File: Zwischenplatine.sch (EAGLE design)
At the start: 12 parts

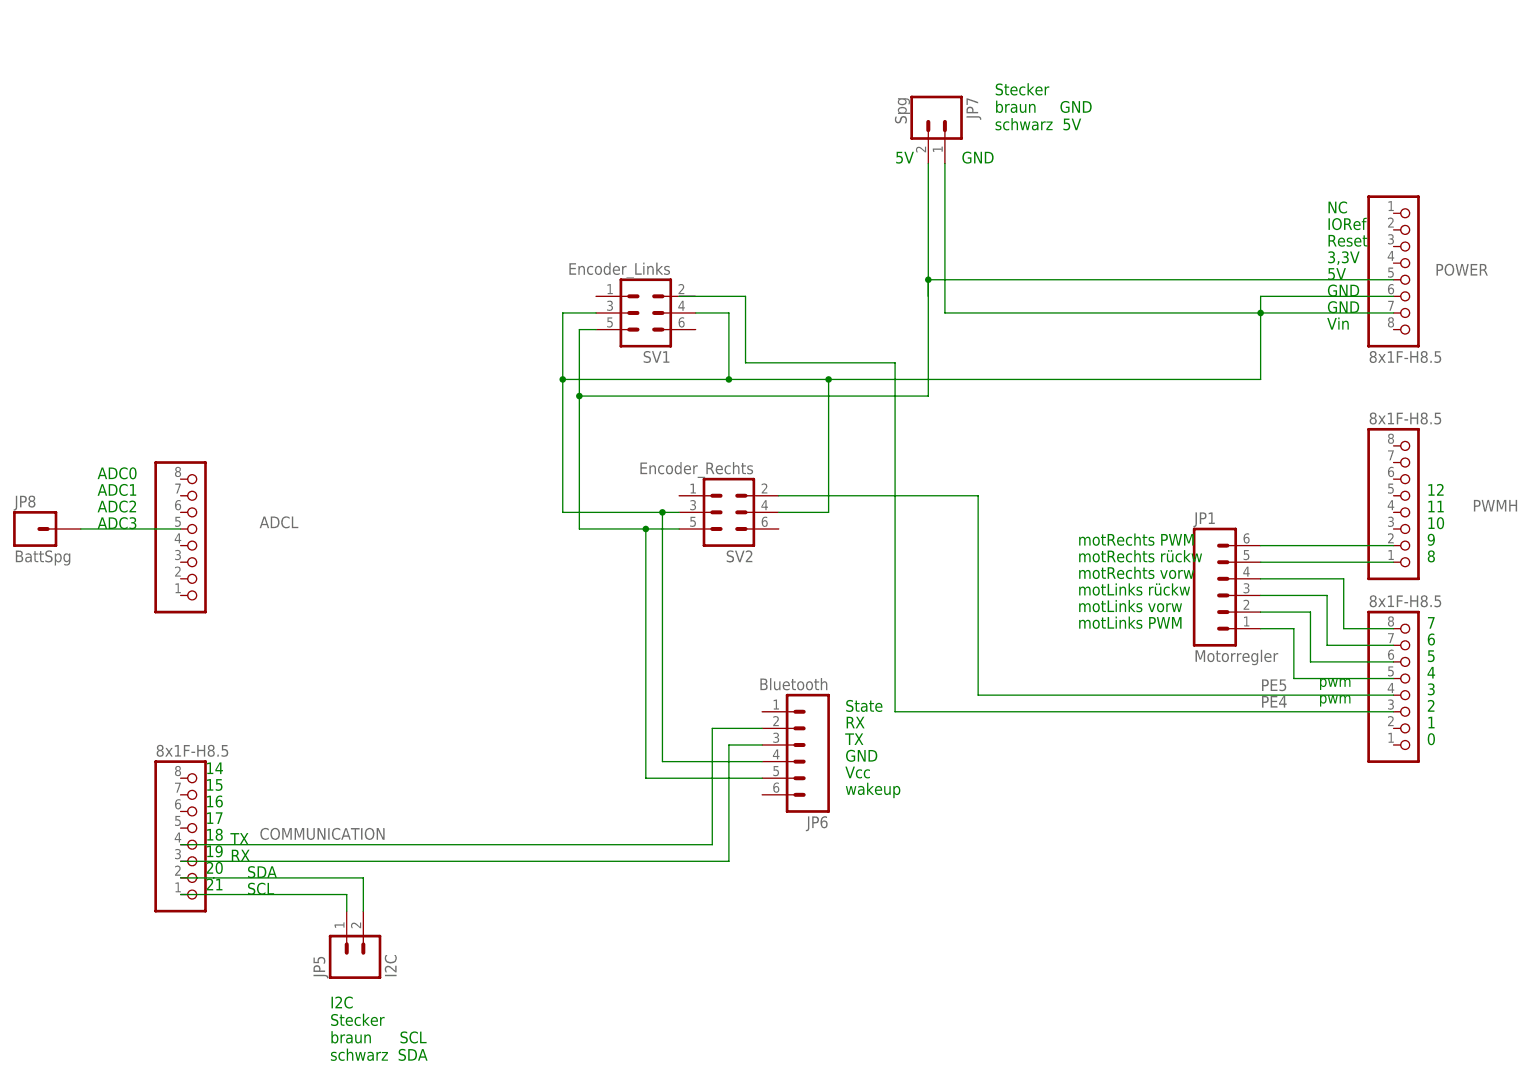
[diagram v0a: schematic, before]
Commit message: 
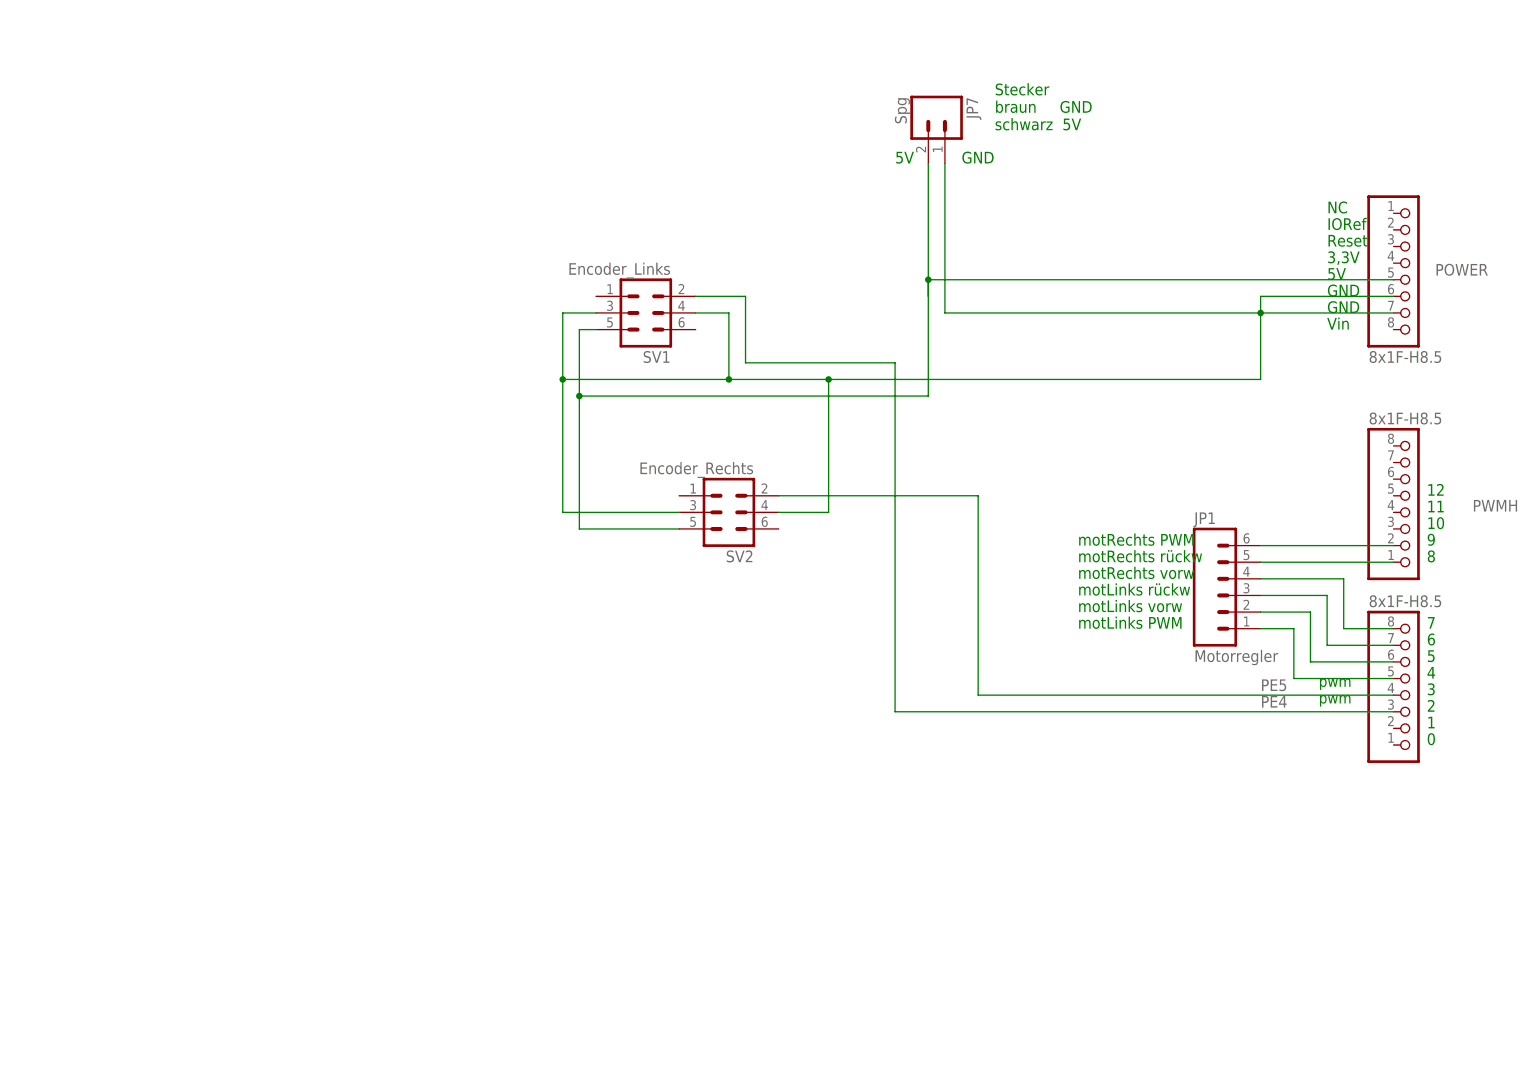
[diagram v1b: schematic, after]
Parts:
- removed ADCL, COMMUNICATION: 8x1F-H8.5, SmartPrj:PINHD-1X8
- removed JP5: I2C, SparkFun-Connectors:M02-JST-2MM-SMT
- removed JP6: Bluetooth, SparkFun-Connectors:M06LOCK
- removed JP8: BattSpg, SparkFun-Connectors:M01PTH
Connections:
- removed net N$10: COMMUNICATION.1, JP5.2
- removed net N$11: COMMUNICATION.2, JP5.1
- removed net N$12: COMMUNICATION.3, JP6.3
- removed net N$13: COMMUNICATION.4, JP6.2
- removed net N$5: ADCL.5, JP8.1
- net N$1: no longer JP6.5
- net N$2: no longer JP6.4
- net PE4: now also SV1.2
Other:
- note removed: "14"
- note removed: "15"
- note removed: "16"
- note removed: "17"
- note removed: "18"
- note removed: "19"
- note removed: "20"
- note removed: "21"
- note removed: "ADC0"
- note removed: "ADC1"
- note removed: "ADC2"
- note removed: "ADC3"
- note removed: "I2C Stecker braun SCL schwarz SDA"
- note removed: "RX"
- note removed: "SCL"
- note removed: "SDA"
- note removed: "State"
- note removed: "TX"
- note removed: "Vcc"
- note removed: "wakeup"
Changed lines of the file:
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@@
 <parts>
 <part name="FRAME1" library="SparkFun-Aesthetics" deviceset="FRAME-A4L" device=""/>
-<part name="JP5" library="SparkFun-Connectors" deviceset="M02" device="-JST-2MM-SMT" value="I2C"/>
-<part name="JP6" library="SparkFun-Connectors" deviceset="M06" device="LOCK" value="Bluetooth"/>
 <part name="SV1" library="con-ml" deviceset="ML6" device="" value="Encoder_Links"/>
 <part name="SV2" library="con-ml" deviceset="ML6" device="" value="Encoder_Rechts"/>
 <part name="JP7" library="SparkFun-Connectors" deviceset="M02" device="-JST-2MM-SMT" value="Spg"/>
-<part name="JP8" library="SparkFun-Connectors" deviceset="M01" device="PTH" value="BattSpg"/>
 <part name="PWML" library="SmartPrj" deviceset="PINHD-1X8" device="" value="8x1F-H8.5"/>
-<part name="ADCL" library="SmartPrj" deviceset="PINHD-1X8" device="" value="8x1F-H8.5"/>
-<part name="COMMUNICATION" library="SmartPrj" deviceset="PINHD-1X8" device="" value="8x1F-H8.5"/>
 <part name="POWER" library="SmartPrj" deviceset="PINHD-1X8" device="" value="8x1F-H8.5"/>
 <part name="PWMH" library="SmartPrj" deviceset="PINHD-1X8" device="" value="8x1F-H8.5"/>
@@
 <text x="134.62" y="66.04" size="1.778" layer="91">6</text>
 <text x="134.62" y="68.58" size="1.778" layer="91">7</text>
-<text x="-52.07" y="43.815" size="1.778" layer="91">15</text>
-<text x="-52.07" y="41.275" size="1.778" layer="91">16</text>
-<text x="-52.07" y="38.735" size="1.778" layer="91">17</text>
-<text x="-52.07" y="36.195" size="1.778" layer="91">18</text>
-<text x="-52.07" y="33.655" size="1.778" layer="91">19</text>
-<text x="-52.07" y="31.115" size="1.778" layer="91">20</text>
-<text x="-52.07" y="28.575" size="1.778" layer="91">21</text>
-<text x="-52.07" y="46.355" size="1.778" layer="91">14</text>
 <text x="118.11" y="57.15" size="1.6764" layer="91">pwm</text>
 <text x="118.11" y="59.69" size="1.6764" layer="91">pwm</text>
@@
 <text x="81.28" y="78.74" size="1.778" layer="91">motRechts rückw</text>
 <text x="81.28" y="81.28" size="1.778" layer="91">motRechts PWM</text>
-<text x="-45.72" y="27.94" size="1.778" layer="91">SCL</text>
-<text x="-45.72" y="30.48" size="1.778" layer="91">SDA</text>
-<text x="45.72" y="43.18" size="1.778" layer="91">wakeup</text>
-<text x="45.72" y="45.72" size="1.778" layer="91">Vcc</text>
-<text x="45.72" y="48.26" size="1.778" layer="91">GND</text>
-<text x="45.72" y="50.8" size="1.778" layer="91">TX</text>
-<text x="45.72" y="53.34" size="1.778" layer="91">RX</text>
-<text x="45.72" y="55.88" size="1.778" layer="91">State</text>
-<text x="-48.26" y="33.02" size="1.778" layer="91">RX</text>
-<text x="-48.26" y="35.56" size="1.778" layer="91">TX</text>
-<text x="-33.02" y="2.54" size="1.778" layer="91">I2C
-Stecker
-braun      SCL
-schwarz  SDA</text>
 <text x="68.58" y="144.78" size="1.778" layer="91">Stecker
 braun     GND
 schwarz  5V</text>
-<text x="-68.58" y="83.82" size="1.778" layer="91">ADC3</text>
-<text x="-68.58" y="91.44" size="1.778" layer="91">ADC0</text>
-<text x="-68.58" y="88.9" size="1.778" layer="91">ADC1</text>
-<text x="-68.58" y="86.36" size="1.778" layer="91">ADC2</text>
 </plain>
 <instances>
 <instance part="FRAME1" gate="G$1" x="-93.98" y="-10.16"/>
-<instance part="JP5" gate="G$1" x="-27.94" y="17.78" rot="R90"/>
-<instance part="JP6" gate="G$1" x="38.1" y="50.8" rot="R180"/>
 <instance part="SV1" gate="1" x="15.24" y="116.84" smashed="yes" rot="R180">
 <attribute name="VALUE" x="19.05" y="124.46" size="1.778" layer="96" rot="R180"/>
@@
 </instance>
 <instance part="JP7" gate="G$1" x="58.42" y="147.32" rot="R270"/>
-<instance part="JP8" gate="G$1" x="-78.74" y="83.82"/>
 <instance part="PWML" gate="A" x="132.08" y="60.96" smashed="yes" rot="MR180">
 <attribute name="VALUE" x="125.73" y="73.66" size="1.778" layer="96" rot="MR180"/>
-</instance>
-<instance part="ADCL" gate="A" x="-53.34" y="83.82" smashed="yes" rot="MR180">
-<attribute name="NAME" x="-43.815" y="85.725" size="1.778" layer="95" rot="MR180"/>
-</instance>
-<instance part="COMMUNICATION" gate="A" x="-53.34" y="38.1" smashed="yes" rot="MR180">
-<attribute name="NAME" x="-43.815" y="38.1" size="1.778" layer="95" rot="MR180"/>
-<attribute name="VALUE" x="-59.69" y="50.8" size="1.778" layer="96" rot="MR180"/>
 </instance>
 <instance part="POWER" gate="A" x="132.08" y="121.92" smashed="yes">
@@
 <label x="109.22" y="56.515" size="1.778" layer="95"/>
 <pinref part="PWML" gate="A" pin="3"/>
-<wire x1="20.32" y1="119.38" x2="30.48" y2="119.38" width="0.1524" layer="91"/>
 <wire x1="30.48" y1="119.38" x2="30.48" y2="109.22" width="0.1524" layer="91"/>
 <wire x1="30.48" y1="109.22" x2="53.34" y2="109.22" width="0.1524" layer="91"/>
 <wire x1="53.34" y1="109.22" x2="53.34" y2="55.88" width="0.1524" layer="91"/>
+<pinref part="SV1" gate="1" pin="2"/>
+<wire x1="30.48" y1="119.38" x2="22.86" y2="119.38" width="0.1524" layer="91"/>
 </segment>
 </net>
@@
 <wire x1="5.08" y1="114.3" x2="5.08" y2="104.14" width="0.1524" layer="91"/>
 <wire x1="5.08" y1="104.14" x2="5.08" y2="83.82" width="0.1524" layer="91"/>
-<wire x1="5.08" y1="83.82" x2="15.24" y2="83.82" width="0.1524" layer="91"/>
+<wire x1="5.08" y1="83.82" x2="20.32" y2="83.82" width="0.1524" layer="91"/>
 <wire x1="58.42" y1="104.14" x2="5.08" y2="104.14" width="0.1524" layer="91"/>
 <junction x="5.08" y="104.14"/>
-<wire x1="15.24" y1="83.82" x2="15.24" y2="45.72" width="0.1524" layer="91"/>
 <pinref part="JP7" gate="G$1" pin="1"/>
 <pinref part="POWER" gate="A" pin="5"/>
@@
 <wire x1="58.42" y1="121.92" x2="58.42" y2="119.38" width="0.1524" layer="91"/>
 <junction x="58.42" y="121.92"/>
-<pinref part="JP6" gate="G$1" pin="5"/>
-<wire x1="33.02" y1="45.72" x2="15.24" y2="45.72" width="0.1524" layer="91"/>
 <pinref part="SV1" gate="1" pin="5"/>
 <wire x1="7.62" y1="114.3" x2="5.08" y2="114.3" width="0.1524" layer="91"/>
 <pinref part="SV2" gate="1" pin="5"/>
-<wire x1="20.32" y1="83.82" x2="15.24" y2="83.82" width="0.1524" layer="91"/>
-<junction x="15.24" y="83.82"/>
 </segment>
 </net>
@@
 <wire x1="27.94" y1="116.84" x2="27.94" y2="106.68" width="0.1524" layer="91"/>
 <wire x1="2.54" y1="106.68" x2="2.54" y2="86.36" width="0.1524" layer="91"/>
-<wire x1="2.54" y1="86.36" x2="17.78" y2="86.36" width="0.1524" layer="91"/>
+<wire x1="2.54" y1="86.36" x2="20.32" y2="86.36" width="0.1524" layer="91"/>
 <wire x1="43.18" y1="86.36" x2="43.18" y2="106.68" width="0.1524" layer="91"/>
 <junction x="2.54" y="106.68"/>
 <junction x="27.94" y="106.68"/>
 <junction x="43.18" y="106.68"/>
-<wire x1="17.78" y1="86.36" x2="17.78" y2="48.26" width="0.1524" layer="91"/>
 <pinref part="JP7" gate="G$1" pin="2"/>
-<pinref part="JP6" gate="G$1" pin="4"/>
-<wire x1="33.02" y1="48.26" x2="17.78" y2="48.26" width="0.1524" layer="91"/>
 <pinref part="SV1" gate="1" pin="4"/>
 <wire x1="27.94" y1="116.84" x2="22.86" y2="116.84" width="0.1524" layer="91"/>
 <pinref part="SV2" gate="1" pin="3"/>
-<wire x1="20.32" y1="86.36" x2="17.78" y2="86.36" width="0.1524" layer="91"/>
-<junction x="17.78" y="86.36"/>
 <pinref part="SV2" gate="1" pin="4"/>
 <wire x1="43.18" y1="86.36" x2="35.56" y2="86.36" width="0.1524" layer="91"/>
-</segment>
-</net>
-<net name="N$10" class="0">
-<segment>
-<wire x1="-30.48" y1="27.94" x2="-30.48" y2="25.4" width="0.1524" layer="91"/>
-<pinref part="JP5" gate="G$1" pin="2"/>
-<pinref part="COMMUNICATION" gate="A" pin="1"/>
-<wire x1="-55.88" y1="27.94" x2="-30.48" y2="27.94" width="0.1524" layer="91"/>
-</segment>
-</net>
-<net name="N$11" class="0">
-<segment>
-<wire x1="-53.34" y1="30.48" x2="-50.8" y2="30.48" width="0.1524" layer="91"/>
-<wire x1="-50.8" y1="30.48" x2="-27.94" y2="30.48" width="0.1524" layer="91"/>
-<wire x1="-27.94" y1="30.48" x2="-27.94" y2="25.4" width="0.1524" layer="91"/>
-<pinref part="JP5" gate="G$1" pin="1"/>
-<pinref part="COMMUNICATION" gate="A" pin="2"/>
-<wire x1="-55.88" y1="30.48" x2="-53.34" y2="30.48" width="0.1524" layer="91"/>
-</segment>
-</net>
-<net name="N$12" class="0">
-<segment>
-<wire x1="-55.88" y1="33.02" x2="27.94" y2="33.02" width="0.1524" layer="91"/>
-<wire x1="27.94" y1="33.02" x2="27.94" y2="50.8" width="0.1524" layer="91"/>
-<pinref part="COMMUNICATION" gate="A" pin="3"/>
-<pinref part="JP6" gate="G$1" pin="3"/>
-<wire x1="27.94" y1="50.8" x2="33.02" y2="50.8" width="0.1524" layer="91"/>
-</segment>
-</net>
-<net name="N$13" class="0">
-<segment>
-<wire x1="-55.88" y1="35.56" x2="25.4" y2="35.56" width="0.1524" layer="91"/>
-<wire x1="25.4" y1="35.56" x2="25.4" y2="53.34" width="0.1524" layer="91"/>
-<pinref part="COMMUNICATION" gate="A" pin="4"/>
-<pinref part="JP6" gate="G$1" pin="2"/>
-<wire x1="25.4" y1="53.34" x2="33.02" y2="53.34" width="0.1524" layer="91"/>
 </segment>
 </net>
@@
 </segment>
 </net>
-<net name="N$5" class="0">
-<segment>
-<pinref part="JP8" gate="G$1" pin="1"/>
-<pinref part="ADCL" gate="A" pin="5"/>
-<wire x1="-71.12" y1="83.82" x2="-55.88" y2="83.82" width="0.1524" layer="91"/>
-</segment>
-</net>
